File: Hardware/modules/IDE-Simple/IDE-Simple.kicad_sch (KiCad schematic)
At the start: 9 parts, among them J1 Conn_02x20_Odd_Even, J2 Conn_02x22_Odd_Even, J3 Bus_PCI_6502, U1 74HC138, U2 74AHC2G00

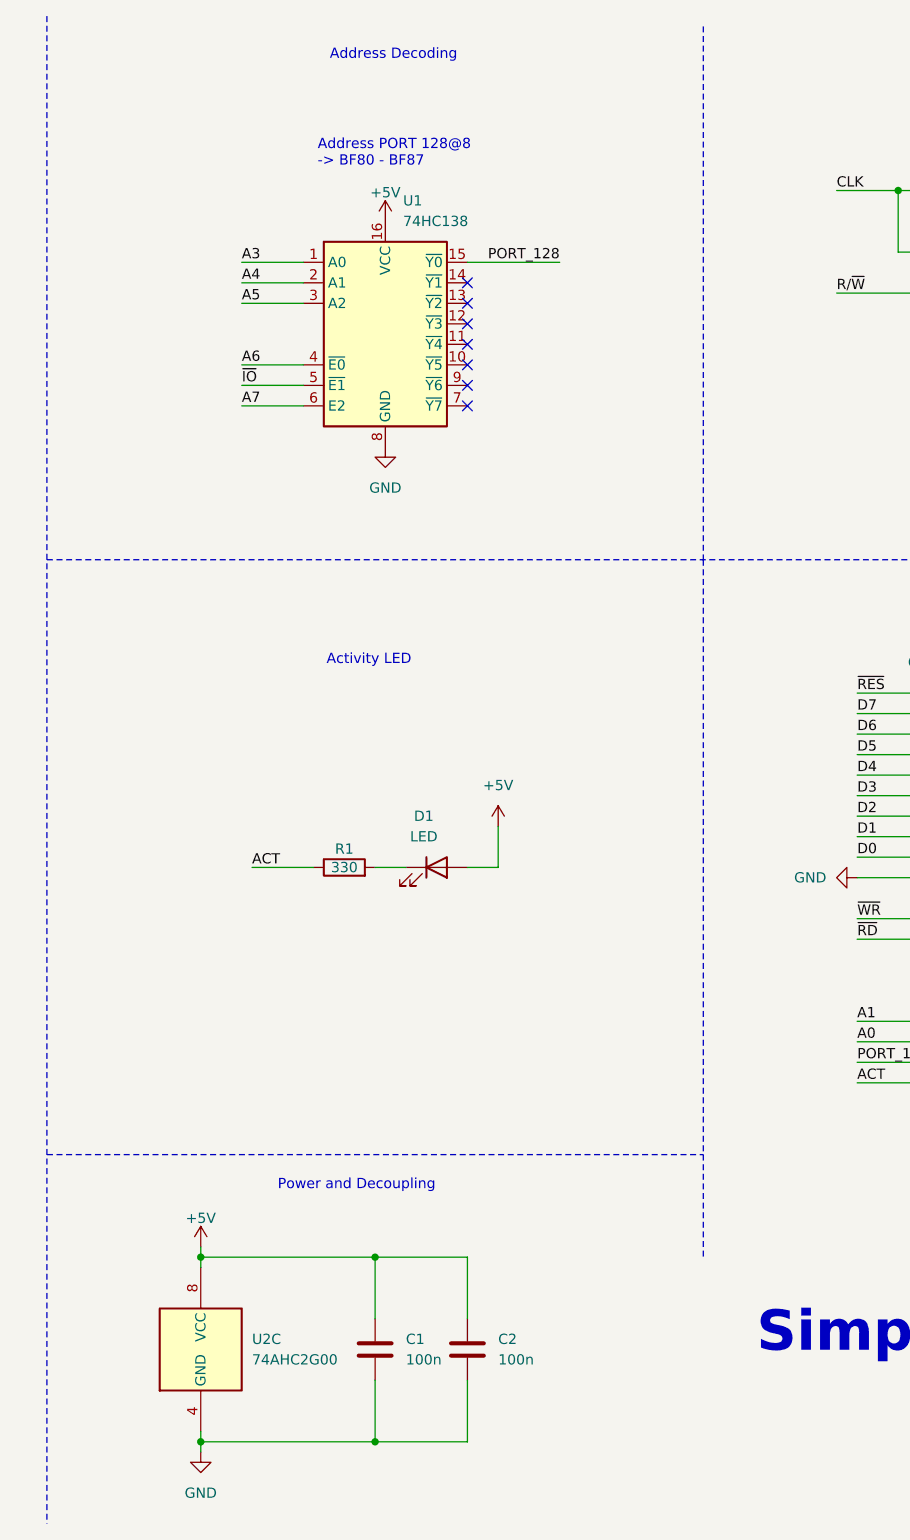
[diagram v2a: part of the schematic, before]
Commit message: Hardware Review Pt. 1 fix Address Decoding for Strobe Generators add bulk capacitance to every board fix wiring of Prototyping Board
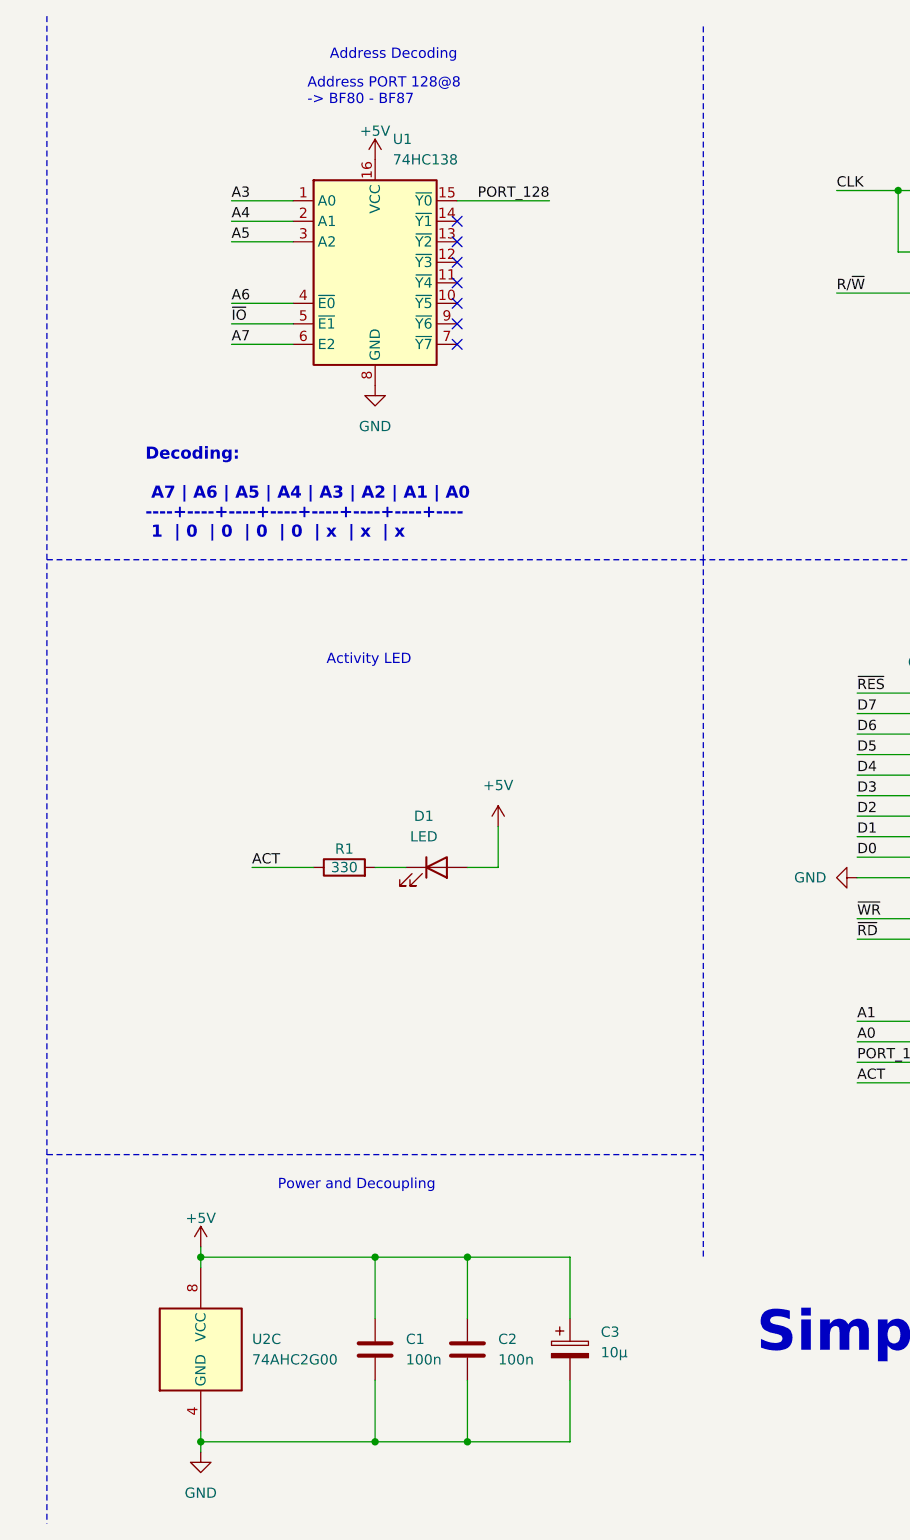
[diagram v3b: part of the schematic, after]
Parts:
- added C3: 10µ, Capacitor_THT:CP_Radial_D5.0mm_P2.50mm, symbol Device:C_Polarized
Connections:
- net +5V: now also C3.1
- net GND: now also C3.2
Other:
- note added: "Decoding: A7 | A6 | A5 | A4 | A3 | A2 | A1 | A0 ----+----+----+----+----+----+----+---- 1 | 0 | 0 | 0 | 0 | x | x | x"
- moved on the sheet: U1
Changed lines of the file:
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@@
 	)
 	(junction
+		(at 148.59 187.96)
+		(diameter 0)
+		(color 0 0 0 0)
+	)
+	(junction
 		(at 220.98 125.73)
 		(diameter 0)
@@
 	)
 	(junction
+		(at 148.59 165.1)
+		(diameter 0)
+		(color 0 0 0 0)
+	)
+	(junction
 		(at 233.68 43.18)
 		(diameter 0)
@@
 	)
 	(no_connect
-		(at 148.59 46.99)
+		(at 147.32 39.37)
 	)
 	(no_connect
@@
 	)
 	(no_connect
-		(at 148.59 52.07)
+		(at 147.32 44.45)
 	)
 	(no_connect
@@
 	)
 	(no_connect
-		(at 148.59 54.61)
+		(at 147.32 46.99)
 	)
 	(no_connect
@@
 	)
 	(no_connect
-		(at 148.59 44.45)
+		(at 147.32 36.83)
 	)
 	(no_connect
@@
 	)
 	(no_connect
-		(at 148.59 59.69)
+		(at 147.32 52.07)
 	)
 	(no_connect
@@
 	)
 	(no_connect
-		(at 148.59 57.15)
+		(at 147.32 49.53)
 	)
 	(no_connect
@@
 	)
 	(no_connect
-		(at 148.59 49.53)
+		(at 147.32 41.91)
 	)
 	(no_connect
@@
 	(wire
 		(pts
-			(xy 148.59 41.91) (xy 160.02 41.91)
+			(xy 147.32 34.29) (xy 158.75 34.29)
 		)
 		(stroke
@@
 	(wire
 		(pts
+			(xy 161.29 180.34) (xy 161.29 187.96)
+		)
+		(stroke
+			(width 0)
+			(type default)
+		)
+	)
+	(wire
+		(pts
 			(xy 220.98 95.25) (xy 219.71 95.25)
 		)
@@
 	(wire
 		(pts
-			(xy 120.65 57.15) (xy 128.27 57.15)
+			(xy 119.38 49.53) (xy 127 49.53)
 		)
 		(stroke
@@
 	(wire
 		(pts
-			(xy 120.65 41.91) (xy 128.27 41.91)
+			(xy 119.38 34.29) (xy 127 34.29)
 		)
 		(stroke
@@
 	(wire
 		(pts
-			(xy 120.65 54.61) (xy 128.27 54.61)
+			(xy 119.38 46.99) (xy 127 46.99)
 		)
 		(stroke
@@
 	(wire
 		(pts
-			(xy 120.65 59.69) (xy 128.27 59.69)
+			(xy 119.38 52.07) (xy 127 52.07)
 		)
 		(stroke
@@
 	(wire
 		(pts
+			(xy 161.29 172.72) (xy 161.29 165.1)
+		)
+		(stroke
+			(width 0)
+			(type default)
+		)
+	)
+	(wire
+		(pts
 			(xy 240.03 102.87) (xy 250.19 102.87)
 		)
@@
 	(wire
 		(pts
+			(xy 161.29 187.96) (xy 148.59 187.96)
+		)
+		(stroke
+			(width 0)
+			(type default)
+		)
+	)
+	(wire
+		(pts
 			(xy 27.94 29.21) (xy 33.02 29.21)
 		)
@@
 	(wire
 		(pts
-			(xy 120.65 46.99) (xy 128.27 46.99)
+			(xy 119.38 39.37) (xy 127 39.37)
 		)
 		(stroke
@@
 	(wire
 		(pts
+			(xy 161.29 165.1) (xy 148.59 165.1)
+		)
+		(stroke
+			(width 0)
+			(type default)
+		)
+	)
+	(wire
+		(pts
 			(xy 80.01 115.57) (xy 68.58 115.57)
 		)
@@
 	(wire
 		(pts
-			(xy 120.65 44.45) (xy 128.27 44.45)
+			(xy 119.38 36.83) (xy 127 36.83)
 		)
 		(stroke
@@
 	(text "Address PORT 128@8\n-> BF80 - BF87"
 		(exclude_from_sim no)
-		(at 130.048 28.448 0)
+		(at 128.778 20.828 0)
 		(effects
 			(font
@@
 		)
 	)
+	(text "Decoding:\n\n A7 | A6 | A5 | A4 | A3 | A2 | A1 | A0\n----+----+----+----+----+----+----+----\n 1  | 0  | 0  | 0  | 0  | x  | x  | x"
+		(exclude_from_sim no)
+		(at 108.712 70.612 0)
+		(effects
+			(font
+				(face "DejaVu Sans Mono")
+				(size 1.5 1.5)
+				(thickness 0.254)
+				(bold yes)
+			)
+			(justify left)
+		)
+	)
 	(text "IDE Connectors"
 		(exclude_from_sim no)
@@
 	)
 	(label "A5"
-		(at 120.65 46.99 0)
+		(at 119.38 39.37 0)
 		(fields_autoplaced yes)
 		(effects
@@
 	)
 	(label "A7"
-		(at 120.65 59.69 0)
+		(at 119.38 52.07 0)
 		(fields_autoplaced yes)
 		(effects
@@
 	)
 	(label "A4"
-		(at 120.65 44.45 0)
+		(at 119.38 36.83 0)
 		(fields_autoplaced yes)
 		(effects
@@
 	)
 	(label "PORT_128"
-		(at 160.02 41.91 180)
+		(at 158.75 34.29 180)
 		(fields_autoplaced yes)
 		(effects
@@
 	)
 	(label "~{IO}"
-		(at 120.65 57.15 0)
+		(at 119.38 49.53 0)
 		(fields_autoplaced yes)
 		(effects
@@
 	)
 	(label "A6"
-		(at 120.65 54.61 0)
+		(at 119.38 46.99 0)
 		(fields_autoplaced yes)
 		(effects
@@
 	)
 	(label "A3"
-		(at 120.65 41.91 0)
+		(at 119.38 34.29 0)
 		(fields_autoplaced yes)
 		(effects
@@
 	(symbol
 		(lib_id "74xx:74HC138")
-		(at 138.43 52.07 0)
+		(at 137.16 44.45 0)
 		(unit 1)
 		(exclude_from_sim no)
@@
 		(dnp no)
 		(property "Reference" "U1"
-			(at 140.6241 34.29 0)
+			(at 139.3541 26.67 0)
 			(effects
 				(font
@@
 		)
 		(property "Value" "74HC138"
-			(at 140.6241 36.83 0)
+			(at 139.3541 29.21 0)
 			(effects
 				(font
@@
 		)
 		(property "Footprint" "Package_DIP:DIP-16_W7.62mm"
-			(at 138.43 52.07 0)
+			(at 137.16 44.45 0)
 			(effects
 				(font
@@
 		)
 		(property "Datasheet" "http://www.ti.com/lit/ds/symlink/cd74hc238.pdf"
-			(at 138.43 52.07 0)
+			(at 137.16 44.45 0)
 			(effects
 				(font
@@
 		)
 		(property "Description" "3-to-8 line decoder/multiplexer inverting, DIP-16/SOIC-16/SSOP-16"
-			(at 138.43 52.07 0)
+			(at 137.16 44.45 0)
 			(effects
 				(font
@@
 	(symbol
 		(lib_id "power:GND")
-		(at 138.43 64.77 0)
+		(at 137.16 57.15 0)
 		(mirror y)
 		(unit 1)
@@
 		(fields_autoplaced yes)
 		(property "Reference" "#PWR010"
-			(at 138.43 71.12 0)
+			(at 137.16 63.5 0)
 			(effects
 				(font
@@
 		)
 		(property "Value" "GND"
-			(at 138.43 69.85 0)
+			(at 137.16 62.23 0)
 			(effects
 				(font
@@
 		)
 		(property "Footprint" ""
-			(at 138.43 64.77 0)
+			(at 137.16 57.15 0)
 			(effects
 				(font
@@
 		)
 		(property "Datasheet" ""
-			(at 138.43 64.77 0)
+			(at 137.16 57.15 0)
 			(effects
 				(font
@@
 		)
 		(property "Description" "Power symbol creates a global label with name \"GND\" , ground"
-			(at 138.43 64.77 0)
+			(at 137.16 57.15 0)
 			(effects
 				(font
@@
 	(symbol
 		(lib_id "power:+5V")
-		(at 138.43 36.83 0)
+		(at 137.16 29.21 0)
 		(mirror y)
 		(unit 1)
@@
 		(dnp no)
 		(property "Reference" "#PWR01"
-			(at 138.43 40.64 0)
+			(at 137.16 33.02 0)
 			(effects
 				(font
@@
 		)
 		(property "Value" "+5V"
-			(at 138.43 33.274 0)
+			(at 137.16 25.654 0)
 			(effects
 				(font
@@
 		)
 		(property "Footprint" ""
-			(at 138.43 36.83 0)
+			(at 137.16 29.21 0)
 			(effects
 				(font
@@
 		)
 		(property "Datasheet" ""
-			(at 138.43 36.83 0)
+			(at 137.16 29.21 0)
 			(effects
 				(font
@@
 		)
 		(property "Description" "Power symbol creates a global label with name \"+5V\""
-			(at 138.43 36.83 0)
+			(at 137.16 29.21 0)
 			(effects
 				(font
@@
 	)
 	(symbol
+		(lib_id "Device:C_Polarized")
+		(at 161.29 176.53 0)
+		(unit 1)
+		(exclude_from_sim no)
+		(in_bom yes)
+		(on_board yes)
+		(dnp no)
+		(fields_autoplaced yes)
+		(property "Reference" "C3"
+			(at 165.1 174.3709 0)
+			(effects
+				(font
+					(size 1.27 1.27)
+				)
+				(justify left)
+			)
+		)
+		(property "Value" "10µ"
+			(at 165.1 176.9109 0)
+			(effects
+				(font
+					(size 1.27 1.27)
+				)
+				(justify left)
+			)
+		)
+		(property "Footprint" "Capacitor_THT:CP_Radial_D5.0mm_P2.50mm"
+			(at 162.2552 180.34 0)
+			(effects
+				(font
+					(size 1.27 1.27)
+				)
+				(hide yes)
+			)
+		)
+		(property "Datasheet" "~"
+			(at 161.29 176.53 0)
+			(effects
+				(font
+					(size 1.27 1.27)
+				)
+				(hide yes)
+			)
+		)
+		(property "Description" "Polarized capacitor"
+			(at 161.29 176.53 0)
+			(effects
+				(font
+					(size 1.27 1.27)
+				)
+				(hide yes)
+			)
+		)
+		(pin "1"
+		)
+		(pin "2"
+		)
+		(instances
+			(project ""
+				(path "/6555ffc8-6c1b-43e3-85dd-8b8a3124067a"
+					(reference "C3")
+					(unit 1)
+				)
+			)
+		)
+	)
+	(symbol
 		(lib_id "power:GND")
 		(at 80.01 156.21 90)
@@
 		)
 	)
+	(sheet_instances
+		(path "/"
+			(page "1")
+		)
+	)
